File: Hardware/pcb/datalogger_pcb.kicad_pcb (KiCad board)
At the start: 2 copper layers, 127.5 x 123.3 mm, 50 parts, among them J1 Micro_SD_Card_Det2, J2 Switch OUT, SW1 SW_Wuerth_450301014042, SW2 SW_Push, U1 DS3231MZ, U2 SN74LVC2G00DCTR

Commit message: Corrected errors in PCB
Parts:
- added 10k: 10k, Resistor_SMD:R_0805_2012Metric_Pad1.20x1.40mm_HandSolder, F.Cu at (132.0, 72.7)
- P Mosfet: renamed from P_MOSFET1
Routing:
- net +5V: track 75.5 -> 84.6 mm
- net GND: track 0.00 -> 3.53 mm, vias 4 -> 5
- net /CS: track 85.6 -> 82.1 mm
- net /Batt+: track 25.2 -> 28.3 mm
- net Net-(P_MOSFET1-G): track 20.8 -> 22.4 mm
- net +3.3V: track 424.0 -> 425.5 mm
- net /SCK: track 92.7 -> 93.4 mm
- net /MOSI: track 97.5 -> 98.1 mm
- net /MISO: track 80.8 -> 81.4 mm
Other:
- board text added: "NEX404"
- board text removed: "NEX40400ADAZ"

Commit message: Changed small error in jst SDA and SCL mixup
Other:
- board text added: "SCL SDA"
- board text removed: "SDA SCL"
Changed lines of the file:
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@@
 		)
 	)
-	(gr_text "SDA SCL"
-		(at 55.1 99.9 0)
+	(gr_text "SCL SDA"
+		(at 55.85 100 0)
 		(layer "F.SilkS")
 		(effects
@@
 		)
 	)
-	(gr_text "SDA SCL"
+	(gr_text "SCL SDA"
 		(at 85.7 100.3 0)
 		(layer "F.SilkS")

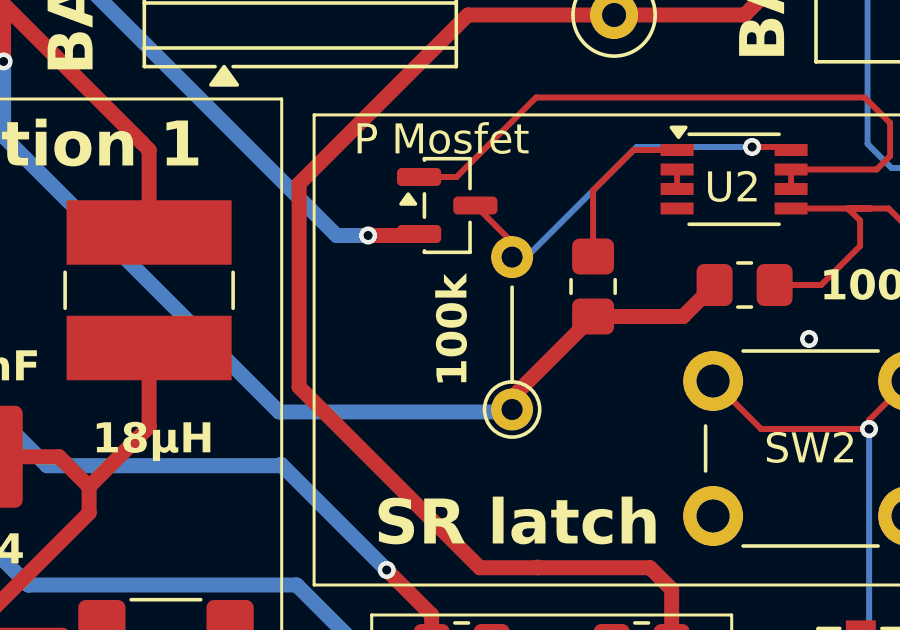
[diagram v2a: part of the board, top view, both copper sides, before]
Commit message: Changes to PCB and new sensor TMP1826 added
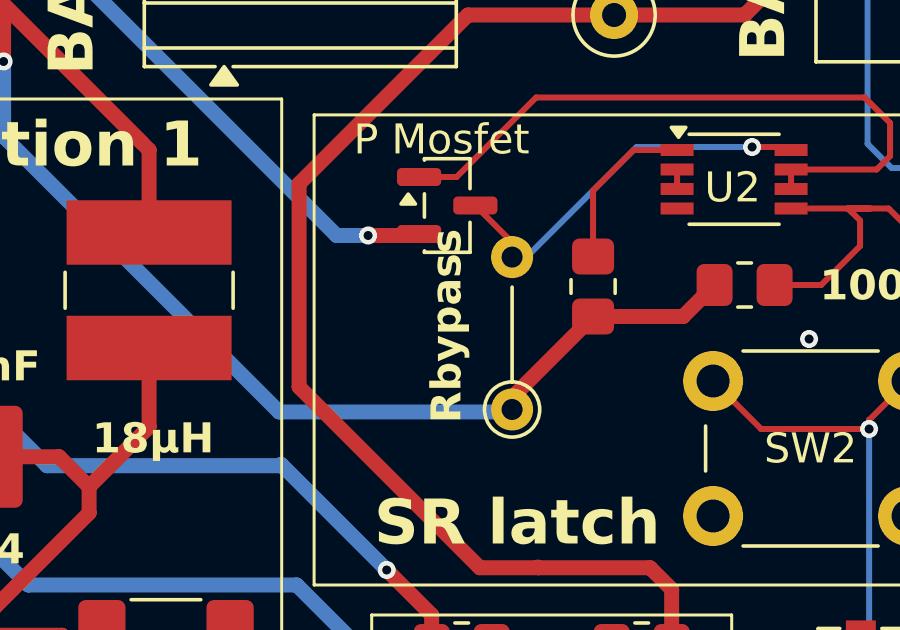
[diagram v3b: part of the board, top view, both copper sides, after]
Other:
- board text added: "Rbypass"
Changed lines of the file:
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@@
 		)
 	)
-	(gr_text "100k"
-		(at 150.2 53.4 90)
+	(gr_text "Rbypass"
+		(at 150 54.6 90)
 		(layer "F.SilkS")
 		(effects

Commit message: Improvements to PCB
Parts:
- removed MOSFET_12V1, MOSFET_5V1: BS170, Package_TO_SOT_THT:TO-92_Inline
- removed R8: 100, Resistor_SMD:R_0805_2012Metric_Pad1.20x1.40mm_HandSolder
- removed R_pdown_MFET_1, R_pdown_MFET_2: 10k, Resistor_SMD:R_0805_2012Metric_Pad1.20x1.40mm_HandSolder
- added 12V: TPS22810DBV, Package_TO_SOT_SMD:SOT-23-6, F.Cu at (171.4, 49.0)
- added 5V: TPS22810DBV, Package_TO_SOT_SMD:SOT-23-6, F.Cu at (171.1, 54.5)
- added C5: 1uF, Capacitor_SMD:C_1812_4532Metric_Pad1.57x3.40mm_HandSolder, F.Cu at (167.1, 45.5)
- added C6: 1uF, Capacitor_SMD:C_1812_4532Metric_Pad1.57x3.40mm_HandSolder, F.Cu at (165.7, 55.6)
- added R6: 10k, Resistor_SMD:R_0805_2012Metric_Pad1.20x1.40mm_HandSolder, F.Cu at (169.9, 57.6)
- P_MOSFET1: renamed from P Mosfet
- Pullup CS: renamed from 10k
- R7: value 100 -> 10k
- R_BYPASS1: footprint Resistor_THT:R_Axial_DIN0204_L3.6mm_D1.6mm_P5.08mm_Vertical -> Resistor_SMD:R_0805_2012Metric_Pad1.20x1.40mm_HandSolder
- moved R7 6.54 mm to (164.9, 49.5), turned to 90 degrees
- moved R_BYPASS1 5.96 mm to (146.6, 50.9)
- moved SW2 4.54 mm to (160.3, 58.6)
- moved R1 4.02 mm to (151.9, 62.0)
- moved R_pullup_shtdwn1 3.15 mm to (156.3, 51.0)
- moved R_pullup_int1 2.52 mm to (151.8, 49.7)
- moved R2 2.52 mm to (147.4, 62.0)
- moved U2 2.25 mm to (156.8, 46.6)
- moved P_MOSFET1 0.65 mm to (148.8, 47.4)
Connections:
- P_MOSFET1 pad 3: Net-(P_MOSFET1-D) -> +5V
- R7 pad 2: Net-(MOSFET_12V1-G) -> GND
- R_BYPASS1 pad 2: Net-(P_MOSFET1-D) -> +5VP
- U2 pad 8: Net-(P_MOSFET1-D) -> +5V
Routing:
- net +12V: track 197.0 -> 98.8 mm
- net Net-(12VSWTCH1-QOD): track 16.5 -> 111.4 mm, vias 0 -> 1
- net Net-(MOSFET_12V1-G): track 93.0 -> 0.00 mm, vias 1 -> 0
- net Net-(5VSWTCH1-QOD): track 14.5 -> 106.4 mm, vias 0 -> 2
- net Net-(MOSFET_5V1-G): track 85.5 -> 0.00 mm, vias 1 -> 0
- net +5VP: track 295.7 -> 228.3 mm, vias 2 -> 3
- net +5V: track 84.6 -> 101.2 mm, vias 1 -> 4
- net Net-(P_MOSFET1-D): track 13.0 -> 0.00 mm, vias 1 -> 0
- net /RTC_INT: track 54.0 -> 48.7 mm, vias 4 -> 3
- net /READ12V: track 94.0 -> 89.2 mm
- net Net-(5VSWTCH1-EN/UVLO): track 140.8 -> 136.1 mm
- net Net-(12VSWTCH1-EN/UVLO): track 120.7 -> 124.4 mm, vias 1 -> 2
- net /I2C0_SDA: track 171.8 -> 174.6 mm
- net /AGND: track 94.3 -> 91.7 mm
- net /CD: track 82.6 -> 83.4 mm
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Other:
- board text added: "1µF"
- board text added: "Datalogger Cocoa-For-Flux"
- board text added: "PWR"
- board text added: "bypass"
- board text removed: "200"
- board text removed: "BS107"
- board text removed: "Datalogger DIAS v2.0"
- board text removed: "MOSFET 12V & 5V"
- board text removed: "PWR option 1"
- board text removed: "Rbypass"
